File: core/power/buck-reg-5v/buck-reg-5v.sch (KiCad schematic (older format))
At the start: 9 parts

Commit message: Laid out reg schematic, made LM25576 symbol, using Molex mega-fit conns
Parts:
- removed P? (x3): CONN_01X02, symbol CONN_01X02
- added C1, C10, C11, C12, C2, C3, C4, C5, C6, C8, C9: C, symbol C
- added C7: CP, symbol CP
- added D1: D_Schottky, symbol D_Schottky
- added L1: INDUCTOR_SMALL, symbol INDUCTOR_SMALL
- added MH1, MH2, MH3, MH4: MOUNTING_HOLE, symbol CONN_01X01
- added P1, P2: MEGA-FIT_02X02, symbol CONN_01X04
- added R1, R2, R3, R4, R5, R6, R7: R, symbol R
- added U1: LM25576, symbol LM25576
- gave numbers to parts that had none: 6
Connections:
- net labels added: BAT_IN, REG_OUT
- net labels removed: 5V_REG, VIN
- wire segments 32 -> 109
- no-connect marks 1 -> 5
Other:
- note added: "Mechanical"
- note added: "Mega-Fit Connectors:\n#0768250004 - 2x2 Male Header (PCB)\n#1716920104 - 2x2 Female Receptacle (Free Hanging)\n#1720630311 - Female Crimp Contact (14-16 AWG)"
- note added: "Regulator Circuit"
- note removed: "Input/Output"
- moved on the sheet: D2, F1, R8, R9, U2

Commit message: Finished schematic. Added component values
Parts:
- removed RV1: POT, symbol POT
- added R?: 3.48K, symbol R
- C1, C2: value C -> 2.2uF
- C10, C12: value C -> 0.01uF
- C11, C8: value C -> DNP
- C3: value C -> 0.47uF
- C4: value C -> 0.022uF
- C5: value C -> 330pF
- C6: value C -> 22uF
- C7: value CP -> 150uF
- C9: value C -> 180pF
- D1: value D_Schottky -> CSHD6-100C
- L1: value INDUCTOR_SMALL -> 33uH
- R1, R2: value R -> DNP
- R3: value R -> 10; Power (none) -> 1W
- R4: value R -> 20.5K
- R5: value R -> 15.4K
- R6: value R -> 49.9K
- R7: value R -> 4.99K
- R8: value R -> 220
- R9: value R -> 2.49K
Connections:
- wire segments 109 -> 141
- no-connect marks 5 -> 4
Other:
- moved on the sheet: C1, C10, C11, C2, C5, C6, C7, C9, L1, R1, R2, R3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

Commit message: Finished part selection, footprints. Added parts to PCB
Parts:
- removed C9: 180pF, symbol C
- removed P1, P2: MEGA-FIT_02X02, symbol CONN_01X04
- added C1: 330pF, Capacitors_SMD:C_0805_HandSoldering, symbol C
- added P1, P2: CONN_01X02, C-BISCUIT:Conn_01x02_5.0mm_Phoenix_1935161, symbol CONN_01X02
- C10: renamed from C5; footprint (none) -> Capacitors_SMD:C_0805_HandSoldering
- C11: renamed from C6; footprint (none) -> Capacitors_SMD:C_1210_HandSoldering
- C12: renamed from C7; footprint (none) -> Capacitors_Tantalum_SMD:TantalC_SizeD_EIA-7343_HandSoldering
- C2: renamed from C10; footprint (none) -> Capacitors_SMD:C_0805_HandSoldering
- C3: renamed from C1; footprint (none) -> Capacitors_SMD:C_1812_HandSoldering
- C4: renamed from C11; footprint (none) -> Capacitors_SMD:C_0805_HandSoldering
- C5: renamed from C8; footprint (none) -> Capacitors_SMD:C_0805_HandSoldering
- C6: renamed from C12; footprint (none) -> Capacitors_SMD:C_0805_HandSoldering
- C7: renamed from C2; footprint (none) -> Capacitors_SMD:C_1812_HandSoldering
- C8: renamed from C3; footprint (none) -> Capacitors_SMD:C_0805_HandSoldering
- C9: renamed from C4; footprint (none) -> Capacitors_SMD:C_0805_HandSoldering
- D1: value CSHD6-100C -> CSHD6-60C; footprint (none) -> TO_SOT_Packages_SMD:TO-252-2Lead
- D2: footprint (none) -> TO_SOT_Packages_SMD:SOT-23_Handsoldering
- F1: footprint (none) -> Resistors_SMD:R_1206_HandSoldering
- L1: footprint (none) -> C-BISCUIT:Inductor_EB_DR127
- MH1, MH2, MH3, MH4: footprint (none) -> C-BISCUIT:Mounting_Hole_M3x0.5L_~Plate~_~Pad~
- R1, R2: footprint (none) -> Resistors_SMD:R_0805_HandSoldering
- R10: renamed from R8; footprint (none) -> Resistors_SMD:R_0805_HandSoldering
- R3: renamed from R4; footprint (none) -> Resistors_SMD:R_0805_HandSoldering
- R4: renamed from R6; footprint (none) -> Resistors_SMD:R_0805_HandSoldering
- R5: renamed from R3; footprint (none) -> Resistors_SMD:R_2512_HandSoldering
- R6: renamed from R?; footprint (none) -> Resistors_SMD:R_0805_HandSoldering
- R7: renamed from R9; footprint (none) -> Resistors_SMD:R_0805_HandSoldering
- R8: renamed from R5; footprint (none) -> Resistors_SMD:R_0805_HandSoldering
- R9: renamed from R7; footprint (none) -> Resistors_SMD:R_0805_HandSoldering
- U1: footprint (none) -> C-BISCUIT:SOIC-20-1EP
- U2: footprint (none) -> TO_SOT_Packages_SMD:TO-252-2Lead
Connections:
- net +5V: now also P1.1 (P1)
- net BAT_IN: now also P2.1 (P1)
- net GND: now also C1.1, P1.2 (P2), P2.2 (P2)
- net at U1.9 (RAMP): now also C1.2
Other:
- note added: "Ceramic Cap Dielectric: X7R"
- note added: "SMD Cap and Res Size: 0805 Hand-Soldered"
- note removed: "Mega-Fit Connectors:\n#0768250004 - 2x2 Male Header (PCB)\n#1716920104 - 2x2 Female Receptacle (Free Hanging)\n#1720630311 - Female Crimp Contact (14-16 AWG)"
- moved on the sheet: MH1, MH2, MH3, MH4, R3

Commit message: Finished buck reg PCB but needs review (and M3 holes)
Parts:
- added W1, W2: TP, Socket_Strips:Socket_Strip_Straight_1x01, symbol TEST_1P
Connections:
- net VCC: now reaches C8.1, U1.1 (VCC)
- net SS: now reaches C2.1, U1.11 (SS)
- net IS: now reaches D1.2 (A), U1.15 (IS), U1.16 (IS)
- net SW: now reaches C10.2, C9.1, D1.1 (K), L1.1, U1.17 (SW), U1.18 (SW), U1.19 (PRE)
- net SD: now reaches C5.1, R1.2, R2.1, U1.2 (SD)
- net SD: now also W1.1
- net BST: now reaches C9.2, U1.20 (BST)
- net SYNC: now reaches U1.5 (SYNC)
- net SYNC: now also W2.1
- net COMP: now reaches C4.1, R4.1, U1.6 (COMP)
- net FB: now reaches C4.2, C6.2, R8.2, R9.1, U1.7 (FB)
- net RT: now reaches R3.1, U1.8 (RT)
- net RAMP: now reaches C1.2, U1.9 (RAMP)
- net REG_OUT renamed OUT
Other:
- moved on the sheet: C9
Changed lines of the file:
@@
 $EndComp
 $Comp
-L GND #PWR15
+L GND #PWR01
 U 1 1 56A29EAD
 P 4950 6150
-F 0 "#PWR15" H 4950 5900 50  0001 C CNN
+F 0 "#PWR01" H 4950 5900 50  0001 C CNN
 F 1 "GND" H 4958 5976 50  0000 C CNN
 F 2 "" H 4950 6150 50  0000 C CNN
@@
 $EndComp
 $Comp
-L +5V #PWR19
+L +5V #PWR02
 U 1 1 56A2C939
 P 6050 5050
-F 0 "#PWR19" H 6050 4900 50  0001 C CNN
+F 0 "#PWR02" H 6050 4900 50  0001 C CNN
 F 1 "+5V" H 6068 5224 50  0000 C CNN
 F 2 "" H 6050 5050 50  0000 C CNN
@@
 Crowbar Circuit
 $Comp
-L +5V #PWR3
+L +5V #PWR03
 U 1 1 56A2DF79
 P 1500 4700
-F 0 "#PWR3" H 1500 4550 50  0001 C CNN
+F 0 "#PWR03" H 1500 4550 50  0001 C CNN
 F 1 "+5V" H 1518 4874 50  0000 C CNN
 F 2 "" H 1500 4700 50  0000 C CNN
@@
 BAT_IN
 $Comp
-L GND #PWR5
+L GND #PWR04
 U 1 1 56A2E387
 P 1500 5650
-F 0 "#PWR5" H 1500 5400 50  0001 C CNN
+F 0 "#PWR04" H 1500 5400 50  0001 C CNN
 F 1 "GND" H 1508 5476 50  0000 C CNN
 F 2 "" H 1500 5650 50  0000 C CNN
@@
 $EndComp
 $Comp
-L GND #PWR12
+L GND #PWR05
 U 1 1 56A67265
 P 3100 1350
-F 0 "#PWR12" H 3100 1100 50  0001 C CNN
+F 0 "#PWR05" H 3100 1100 50  0001 C CNN
 F 1 "GND" H 3108 1176 50  0000 C CNN
 F 2 "" H 3100 1350 50  0000 C CNN
@@
 L C C9
 U 1 1 56A67758
-P 3800 1850
-F 0 "C9" V 3547 1850 50  0000 C CNN
-F 1 "0.022uF" V 3639 1850 50  0000 C CNN
-F 2 "Capacitors_SMD:C_0805_HandSoldering" H 3838 1700 50  0001 C CNN
-F 3 "" H 3800 1850 50  0000 C CNN
-	1    3800 1850
+P 3950 1850
+F 0 "C9" V 3697 1850 50  0000 C CNN
+F 1 "0.022uF" V 3789 1850 50  0000 C CNN
+F 2 "Capacitors_SMD:C_0805_HandSoldering" H 3988 1700 50  0001 C CNN
+F 3 "" H 3950 1850 50  0000 C CNN
+	1    3950 1850
 	0    1    1    0
 $EndComp
@@
 $EndComp
 $Comp
-L GND #PWR14
+L GND #PWR06
 U 1 1 56A68979
 P 4450 2600
-F 0 "#PWR14" H 4450 2350 50  0001 C CNN
+F 0 "#PWR06" H 4450 2350 50  0001 C CNN
 F 1 "GND" H 4458 2426 50  0000 C CNN
 F 2 "" H 4450 2600 50  0000 C CNN
@@
 $EndComp
 $Comp
-L GND #PWR13
+L GND #PWR07
 U 1 1 56A68E42
 P 3500 3300
-F 0 "#PWR13" H 3500 3050 50  0001 C CNN
+F 0 "#PWR07" H 3500 3050 50  0001 C CNN
 F 1 "GND" H 3508 3126 50  0000 C CNN
 F 2 "" H 3500 3300 50  0000 C CNN
@@
 $EndComp
 $Comp
-L GND #PWR11
+L GND #PWR08
 U 1 1 56A69005
 P 2600 3300
-F 0 "#PWR11" H 2600 3050 50  0001 C CNN
+F 0 "#PWR08" H 2600 3050 50  0001 C CNN
 F 1 "GND" H 2608 3126 50  0000 C CNN
 F 2 "" H 2600 3300 50  0000 C CNN
@@
 $EndComp
 $Comp
-L GND #PWR16
+L GND #PWR09
 U 1 1 56A693B6
 P 5200 3550
-F 0 "#PWR16" H 5200 3300 50  0001 C CNN
+F 0 "#PWR09" H 5200 3300 50  0001 C CNN
 F 1 "GND" H 5208 3376 50  0000 C CNN
 F 2 "" H 5200 3550 50  0000 C CNN
@@
 $EndComp
 $Comp
-L GND #PWR17
+L GND #PWR010
 U 1 1 56A69FA4
 P 5400 2250
-F 0 "#PWR17" H 5400 2000 50  0001 C CNN
+F 0 "#PWR010" H 5400 2000 50  0001 C CNN
 F 1 "GND" H 5408 2076 50  0000 C CNN
 F 2 "" H 5400 2250 50  0000 C CNN
@@
 $EndComp
 $Comp
-L GND #PWR18
+L GND #PWR011
 U 1 1 56A6A03F
 P 5850 2250
-F 0 "#PWR18" H 5850 2000 50  0001 C CNN
+F 0 "#PWR011" H 5850 2000 50  0001 C CNN
 F 1 "GND" H 5858 2076 50  0000 C CNN
 F 2 "" H 5850 2250 50  0000 C CNN
@@
 $EndComp
 $Comp
-L PWR_FLAG #FLG1
+L PWR_FLAG #FLG012
 U 1 1 56A6A4BF
 P 6350 1800
-F 0 "#FLG1" H 6350 1895 50  0001 C CNN
+F 0 "#FLG012" H 6350 1895 50  0001 C CNN
 F 1 "PWR_FLAG" H 6350 2024 50  0000 C CNN
 F 2 "" H 6350 1800 50  0000 C CNN
@@
 	3500 1950 3450 1950
 Wire Wire Line
-	3450 2150 3600 2150
-Wire Wire Line
-	3600 2150 3600 1850
-Wire Wire Line
-	3600 1850 3650 1850
-Wire Wire Line
-	3950 1850 4500 1850
-Wire Wire Line
-	4000 2400 4000 1850
+	3450 2150 3750 2150
+Wire Wire Line
+	3750 2150 3750 1850
+Wire Wire Line
+	3750 1850 3800 1850
+Wire Wire Line
+	4100 1850 4500 1850
+Wire Wire Line
+	4200 2400 4200 1850
 Wire Wire Line
 	3450 2750 3500 2750
@@
 Wire Wire Line
 	4450 2250 4450 2200
-Connection ~ 4000 1850
+Connection ~ 4200 1850
 Wire Wire Line
 	4450 1850 4450 1900
@@
 	2650 3050 2450 3050
 Wire Wire Line
-	2450 3850 2450 3050
+	2450 3050 2450 3850
 Wire Wire Line
 	1800 3850 5100 3850
@@
 Connection ~ 2100 3850
 $Comp
-L GND #PWR1
+L GND #PWR013
 U 1 1 56A6F6A4
 P 1000 3200
-F 0 "#PWR1" H 1000 2950 50  0001 C CNN
+F 0 "#PWR013" H 1000 2950 50  0001 C CNN
 F 1 "GND" H 1008 3026 50  0000 C CNN
 F 2 "" H 1000 3200 50  0000 C CNN
@@
 Connection ~ 3500 2450
 Wire Wire Line
-	3500 2400 4000 2400
+	3500 2400 4200 2400
 Connection ~ 3500 2400
 Wire Wire Line
@@
 $EndComp
 $Comp
-L GND #PWR6
+L GND #PWR014
 U 1 1 56A733D0
 P 1550 2300
-F 0 "#PWR6" H 1550 2050 50  0001 C CNN
+F 0 "#PWR014" H 1550 2050 50  0001 C CNN
 F 1 "GND" H 1558 2126 50  0000 C CNN
 F 2 "" H 1550 2300 50  0000 C CNN
@@
 Connection ~ 1550 1900
 Wire Wire Line
-	2650 2350 2250 2350
-Wire Wire Line
-	2250 2350 2250 1900
+	2250 2350 2650 2350
+Wire Wire Line
+	2250 1850 2250 2350
 Connection ~ 1950 1900
 $Comp
-L GND #PWR9
+L GND #PWR015
 U 1 1 56A74314
 P 1950 2300
-F 0 "#PWR9" H 1950 2050 50  0001 C CNN
+F 0 "#PWR015" H 1950 2050 50  0001 C CNN
 F 1 "GND" H 1958 2126 50  0000 C CNN
 F 2 "" H 1950 2300 50  0000 C CNN
@@
 $EndComp
 $Comp
-L GND #PWR8
+L GND #PWR016
 U 1 1 56A74529
 P 1800 1350
-F 0 "#PWR8" H 1800 1100 50  0001 C CNN
+F 0 "#PWR016" H 1800 1100 50  0001 C CNN
 F 1 "GND" H 1808 1176 50  0000 C CNN
 F 2 "" H 1800 1350 50  0000 C CNN
@@
 $EndComp
 $Comp
-L GND #PWR10
+L GND #PWR017
 U 1 1 56A745C0
 P 2250 1350
-F 0 "#PWR10" H 2250 1100 50  0001 C CNN
+F 0 "#PWR017" H 2250 1100 50  0001 C CNN
 F 1 "GND" H 2258 1176 50  0000 C CNN
 F 2 "" H 2250 1350 50  0000 C CNN
@@
 BAT_IN
 $Comp
-L GND #PWR4
+L GND #PWR018
 U 1 1 56A7D140
 P 1500 4900
-F 0 "#PWR4" H 1500 4650 50  0001 C CNN
+F 0 "#PWR018" H 1500 4650 50  0001 C CNN
 F 1 "GND" H 1508 4726 50  0000 C CNN
 F 2 "" H 1500 4900 50  0000 C CNN
@@
 	1550 3150 1550 3200
 $Comp
-L GND #PWR2
+L GND #PWR019
 U 1 1 56A7400A
 P 1300 3200
-F 0 "#PWR2" H 1300 2950 50  0001 C CNN
+F 0 "#PWR019" H 1300 2950 50  0001 C CNN
 F 1 "GND" H 1308 3026 50  0000 C CNN
 F 2 "" H 1300 3200 50  0000 C CNN
@@
 $EndComp
 $Comp
-L GND #PWR7
+L GND #PWR020
 U 1 1 56A7407B
 P 1550 3200
-F 0 "#PWR7" H 1550 2950 50  0001 C CNN
+F 0 "#PWR020" H 1550 2950 50  0001 C CNN
 F 1 "GND" H 1558 3026 50  0000 C CNN
 F 2 "" H 1550 3200 50  0000 C CNN
@@
 	1    0    0    -1
 $EndComp
+Text Label 2600 3050 2    60   ~ 0
+FB
+Text Label 2600 2950 2    60   ~ 0
+COMP
+Text Label 2600 2550 2    60   ~ 0
+RAMP
+Text Label 2600 2650 2    60   ~ 0
+SS
+Text Label 2600 2750 2    60   ~ 0
+RT
+Text Label 2600 2350 2    60   ~ 0
+SD
+$Comp
+L TEST_1P W2
+U 1 1 56AF146F
+P 2350 2100
+F 0 "W2" H 2408 2220 50  0000 L CNN
+F 1 "TP" H 2408 2128 50  0000 L CNN
+F 2 "Socket_Strips:Socket_Strip_Straight_1x01" H 2550 2100 50  0001 C CNN
+F 3 "" H 2550 2100 50  0000 C CNN
+	1    2350 2100
+	1    0    0    -1
+$EndComp
+Wire Wire Line
+	2350 2100 2350 2250
+Wire Wire Line
+	2350 2250 2650 2250
+$Comp
+L TEST_1P W1
+U 1 1 56AF2A2E
+P 2250 1850
+F 0 "W1" H 2308 1970 50  0000 L CNN
+F 1 "TP" H 2308 1878 50  0000 L CNN
+F 2 "Socket_Strips:Socket_Strip_Straight_1x01" H 2308 1832 50  0001 L CNN
+F 3 "" H 2450 1850 50  0000 C CNN
+	1    2250 1850
+	1    0    0    -1
+$EndComp
+Connection ~ 2250 1900
+Text Label 3550 2800 0    60   ~ 0
+IS
+Text Label 3550 2400 0    60   ~ 0
+SW
+Text Label 3550 2150 0    60   ~ 0
+BST
+Text Label 3100 950  0    60   ~ 0
+VCC
+Text Label 2600 2250 2    60   ~ 0
+SYNC
+Text Label 3550 3050 0    60   ~ 0
+OUT
 $EndSCHEMATC

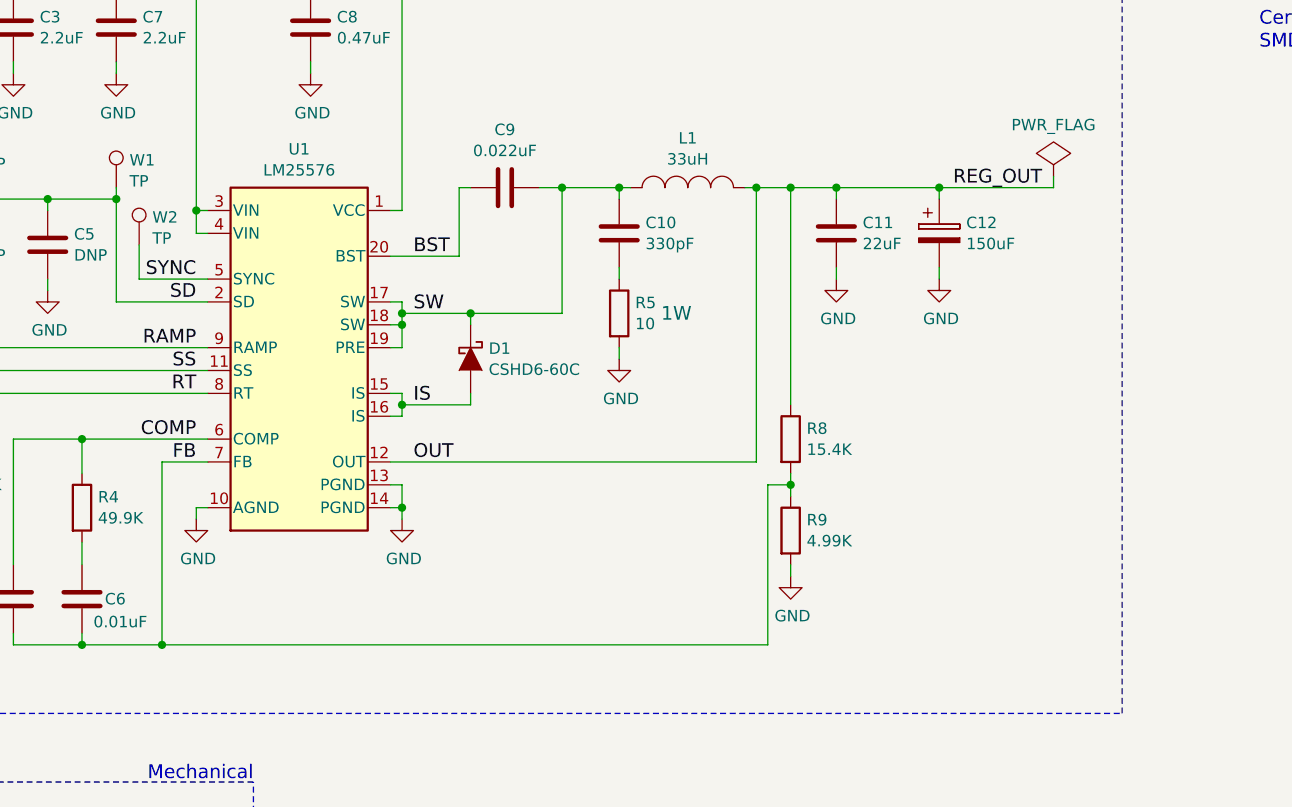
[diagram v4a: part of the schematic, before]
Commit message: Finished buck reg. Awaiting review
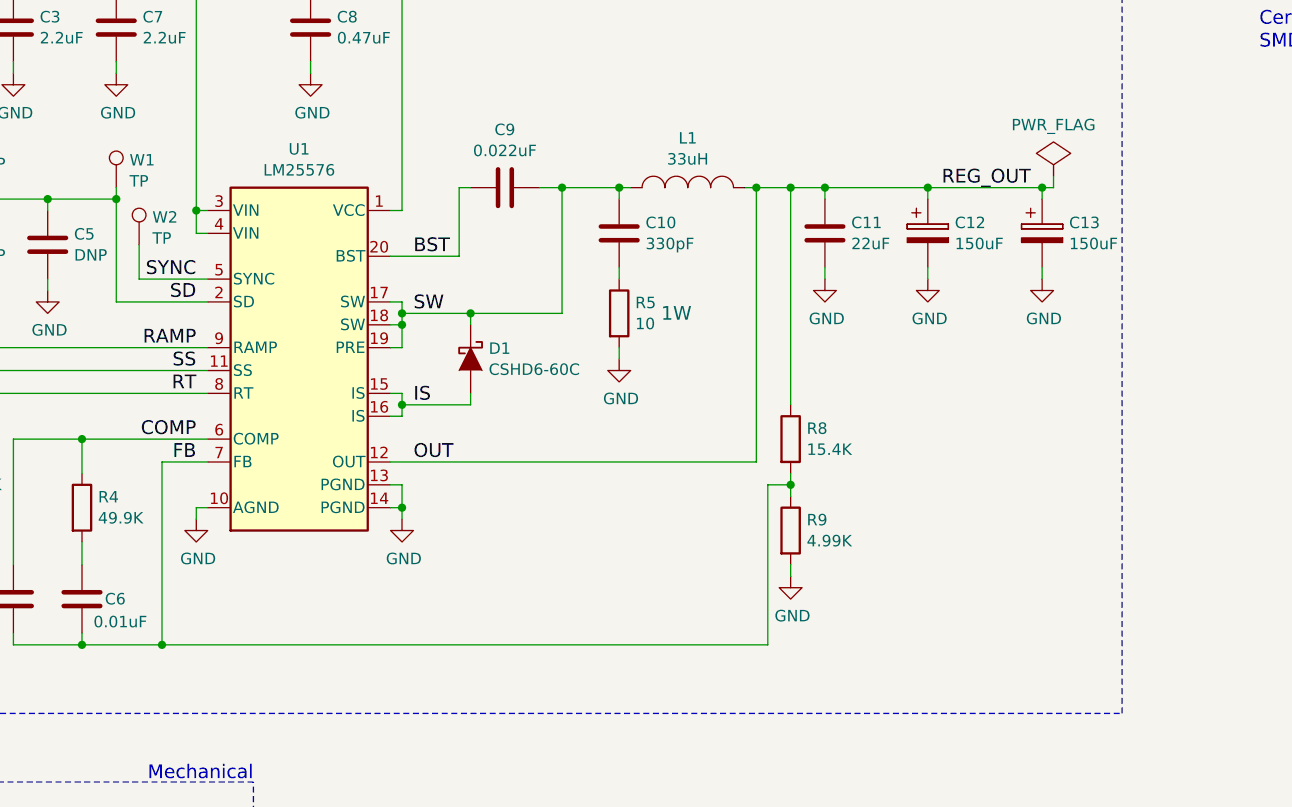
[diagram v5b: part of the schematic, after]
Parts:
- added C13: 150uF, Capacitors_Tantalum_SMD:TantalC_SizeD_EIA-7343_HandSoldering, symbol CP
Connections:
- net GND: now also C13.2
- net OUT: now also C13.1
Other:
- moved on the sheet: C11, C12
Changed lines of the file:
@@
 L C C11
 U 1 1 56A69E44
-P 5400 2050
-F 0 "C11" H 5515 2096 50  0000 L CNN
-F 1 "22uF" H 5515 2004 50  0000 L CNN
-F 2 "Capacitors_SMD:C_1210_HandSoldering" H 5438 1900 50  0001 C CNN
-F 3 "" H 5400 2050 50  0000 C CNN
-	1    5400 2050
+P 5350 2050
+F 0 "C11" H 5465 2096 50  0000 L CNN
+F 1 "22uF" H 5465 2004 50  0000 L CNN
+F 2 "Capacitors_SMD:C_1210_HandSoldering" H 5388 1900 50  0001 C CNN
+F 3 "" H 5350 2050 50  0000 C CNN
+	1    5350 2050
 	1    0    0    -1
 $EndComp
@@
 L CP C12
 U 1 1 56A69EAC
-P 5850 2050
-F 0 "C12" H 5968 2096 50  0000 L CNN
-F 1 "150uF" H 5968 2004 50  0000 L CNN
-F 2 "Capacitors_Tantalum_SMD:TantalC_SizeD_EIA-7343_HandSoldering" H 5888 1900 50  0001 C CNN
-F 3 "" H 5850 2050 50  0000 C CNN
-	1    5850 2050
+P 5800 2050
+F 0 "C12" H 5918 2096 50  0000 L CNN
+F 1 "150uF" H 5918 2004 50  0000 L CNN
+F 2 "Capacitors_Tantalum_SMD:TantalC_SizeD_EIA-7343_HandSoldering" H 5838 1900 50  0001 C CNN
+F 3 "" H 5800 2050 50  0000 C CNN
+	1    5800 2050
 	1    0    0    -1
 $EndComp
@@
 L GND #PWR010
 U 1 1 56A69FA4
-P 5400 2250
-F 0 "#PWR010" H 5400 2000 50  0001 C CNN
-F 1 "GND" H 5408 2076 50  0000 C CNN
-F 2 "" H 5400 2250 50  0000 C CNN
-F 3 "" H 5400 2250 50  0000 C CNN
-	1    5400 2250
+P 5350 2250
+F 0 "#PWR010" H 5350 2000 50  0001 C CNN
+F 1 "GND" H 5358 2076 50  0000 C CNN
+F 2 "" H 5350 2250 50  0000 C CNN
+F 3 "" H 5350 2250 50  0000 C CNN
+	1    5350 2250
 	1    0    0    -1
 $EndComp
@@
 L GND #PWR011
 U 1 1 56A6A03F
-P 5850 2250
-F 0 "#PWR011" H 5850 2000 50  0001 C CNN
-F 1 "GND" H 5858 2076 50  0000 C CNN
-F 2 "" H 5850 2250 50  0000 C CNN
-F 3 "" H 5850 2250 50  0000 C CNN
-	1    5850 2250
+P 5800 2250
+F 0 "#PWR011" H 5800 2000 50  0001 C CNN
+F 1 "GND" H 5808 2076 50  0000 C CNN
+F 2 "" H 5800 2250 50  0000 C CNN
+F 3 "" H 5800 2250 50  0000 C CNN
+	1    5800 2250
 	1    0    0    -1
 $EndComp
@@
 	1    0    0    -1
 $EndComp
-Text Label 6300 1850 2    60   ~ 0
+Text Label 6250 1850 2    60   ~ 0
 REG_OUT
 Text Label 3800 5050 0    60   ~ 0
@@
 	2650 3050 2450 3050
 Wire Wire Line
-	2450 3050 2450 3850
+	2450 3850 2450 3050
 Wire Wire Line
 	1800 3850 5100 3850
@@
 Connection ~ 5050 1850
 Wire Wire Line
-	5400 2250 5400 2200
-Wire Wire Line
-	5850 2250 5850 2200
-Wire Wire Line
-	5400 1850 5400 1900
+	5350 2250 5350 2200
+Wire Wire Line
+	5800 2250 5800 2200
+Wire Wire Line
+	5350 1850 5350 1900
 Connection ~ 5200 1850
 Wire Wire Line
-	5850 1850 5850 1900
-Connection ~ 5400 1850
-Connection ~ 5850 1850
+	5800 1850 5800 1900
+Connection ~ 5350 1850
+Connection ~ 5800 1850
 Wire Wire Line
 	6350 1850 6350 1800
@@
 Text Label 3550 3050 0    60   ~ 0
 OUT
+$Comp
+L CP C13
+U 1 1 56AF7AD0
+P 6300 2050
+F 0 "C13" H 6418 2096 50  0000 L CNN
+F 1 "150uF" H 6418 2004 50  0000 L CNN
+F 2 "Capacitors_Tantalum_SMD:TantalC_SizeD_EIA-7343_HandSoldering" H 6338 1900 50  0001 C CNN
+F 3 "" H 6300 2050 50  0000 C CNN
+	1    6300 2050
+	1    0    0    -1
+$EndComp
+$Comp
+L GND #PWR021
+U 1 1 56AF7B6B
+P 6300 2250
+F 0 "#PWR021" H 6300 2000 50  0001 C CNN
+F 1 "GND" H 6308 2076 50  0000 C CNN
+F 2 "" H 6300 2250 50  0000 C CNN
+F 3 "" H 6300 2250 50  0000 C CNN
+	1    6300 2250
+	1    0    0    -1
+$EndComp
+Wire Wire Line
+	6300 2250 6300 2200
+Wire Wire Line
+	6300 1900 6300 1850
+Connection ~ 6300 1850
 $EndSCHEMATC

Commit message: Added mfg files. Still needs links to parts.
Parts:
- removed D2: LM431, TO_SOT_Packages_SMD:SOT-23_Handsoldering, symbol LM431
- removed F1: 3A, Resistors_SMD:R_1206_HandSoldering, symbol FUSE
- removed MH1, MH2, MH3, MH4: MOUNTING_HOLE, C-BISCUIT:Mounting_Hole_M3x0.5L_~Plate~_~Pad~, symbol CONN_01X01
- removed R10: 220, Resistors_SMD:R_0805_HandSoldering, symbol R
- removed R6: 3.48K, Resistors_SMD:R_0805_HandSoldering, symbol R
- removed R7: 2.49K, Resistors_SMD:R_0805_HandSoldering, symbol R
- removed U2: BT151S-500R, TO_SOT_Packages_SMD:TO-252-2Lead, symbol BT151S-500R
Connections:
- net OUT is gone; now on net +5V: C11.1, C12.1, C13.1, L1.2, R8.1, U1.12 (OUT)
- no-connect marks 4 -> 0
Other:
- note removed: "Crowbar Circuit"
- moved on the sheet: P1, P2
